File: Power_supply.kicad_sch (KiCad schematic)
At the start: 46 parts, among them U100 LM217MDT, U101 AMS1117-3.3, U102 AMS1117-3.3

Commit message: Sch update complete, ERC OK
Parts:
- removed Mod100: WB0524S-1W, Personal:WB___S-1W, symbol personal:WB____S-1W
- removed Mod101: WB0505S-1W, Personal:WB___S-1W, symbol personal:WB____S-1W
- added PS100: B0505S-2W, Personal:DCDC_converter_THT_BxxxxS-2W, symbol personal:B0505S-2W
- added PS101: B0524S-2W, Personal:DCDC_converter_THT_BxxxxS-2W, symbol personal:B0524S-2W
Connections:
- net GND: now also PS100.4 (-Vout)
- net SH0: now also PS100.2 (-Vin), PS101.2 (-Vin), PS101.4 (-Vout)
- net SH24: now also PS101.6 (+Vout)
- net SH5: now also PS100.1 (+Vin), PS101.1 (+Vin)
- net SL5: now also PS100.6 (+Vout)
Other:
- note removed: "Needs to be updated to 2W module"
- moved on the sheet: C100, C103, C105, C106, C108, R100, R101, U100, U102

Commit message: Placement 50%
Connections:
- no-connect marks 0 -> 2
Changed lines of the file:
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@@
 		(color 0 0 0 0)
 	)
+	(no_connect
+		(at 139.7 40.64)
+	)
+	(no_connect
+		(at 139.7 116.84)
+	)
+	(wire
+		(pts
+			(xy 138.43 40.64) (xy 139.7 40.64)
+		)
+		(stroke
+			(width 0)
+			(type default)
+		)
+	)
 	(wire
 		(pts
@@
 		(pts
 			(xy 101.6 74.93) (xy 101.6 76.2)
+		)
+		(stroke
+			(width 0)
+			(type default)
+		)
+	)
+	(wire
+		(pts
+			(xy 138.43 116.84) (xy 139.7 116.84)
 		)
 		(stroke
@@
 			(effects
 				(font
+					(size 1.27 1.27)
+					(italic yes)
+				)
+			)
+		)
+	)
+	(netclass_flag ""
+		(length 2.54)
+		(shape dot)
+		(at 139.7 116.84 270)
+		(effects
+			(font
+				(size 1.27 1.27)
+			)
+			(justify right bottom)
+		)
+		(property "Netclass" "LV"
+			(at 143.51 116.84 0)
+			(effects
+				(font
+					(size 1.27 1.27)
+				)
+				(justify left)
+			)
+		)
+		(property "Component Class" ""
+			(at -85.09 85.09 0)
+			(effects
+				(font

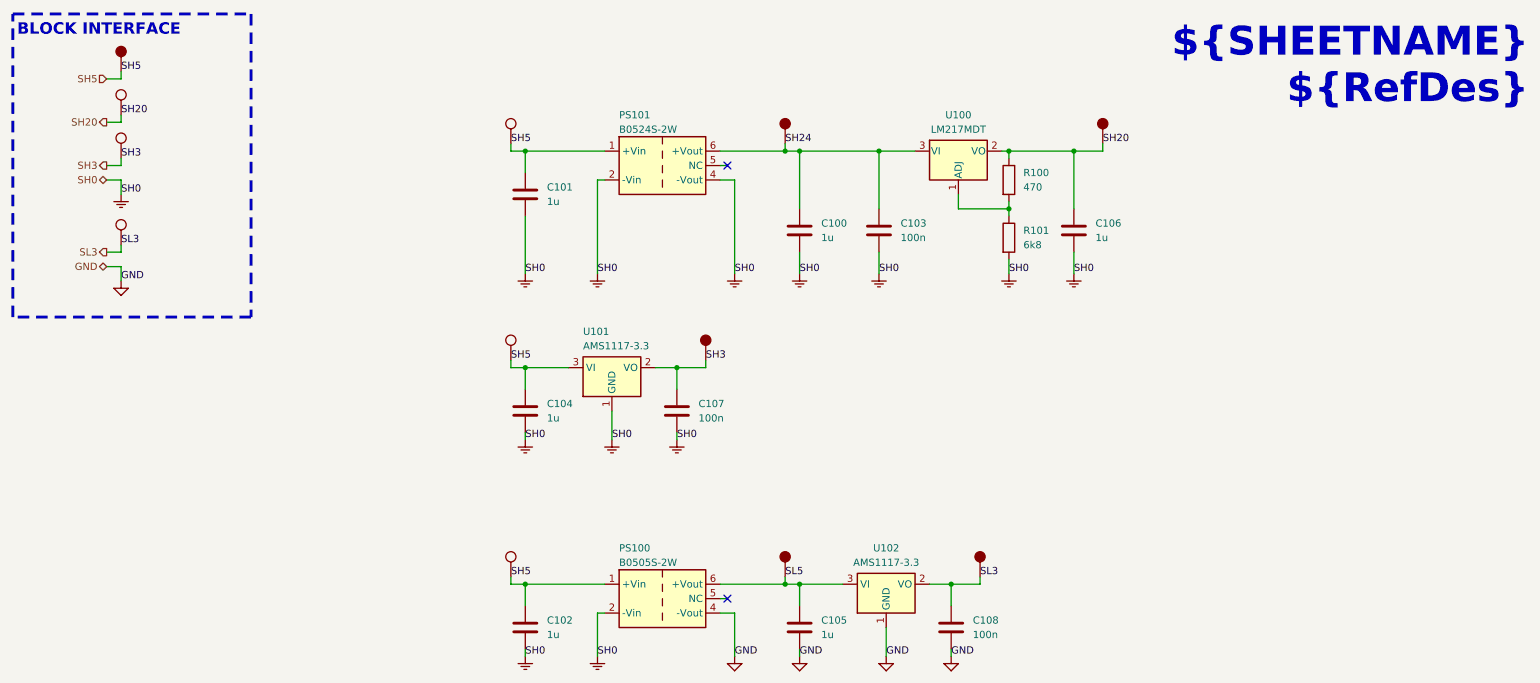
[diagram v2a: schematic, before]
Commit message: Reannotated, silk done, missing some 3D models
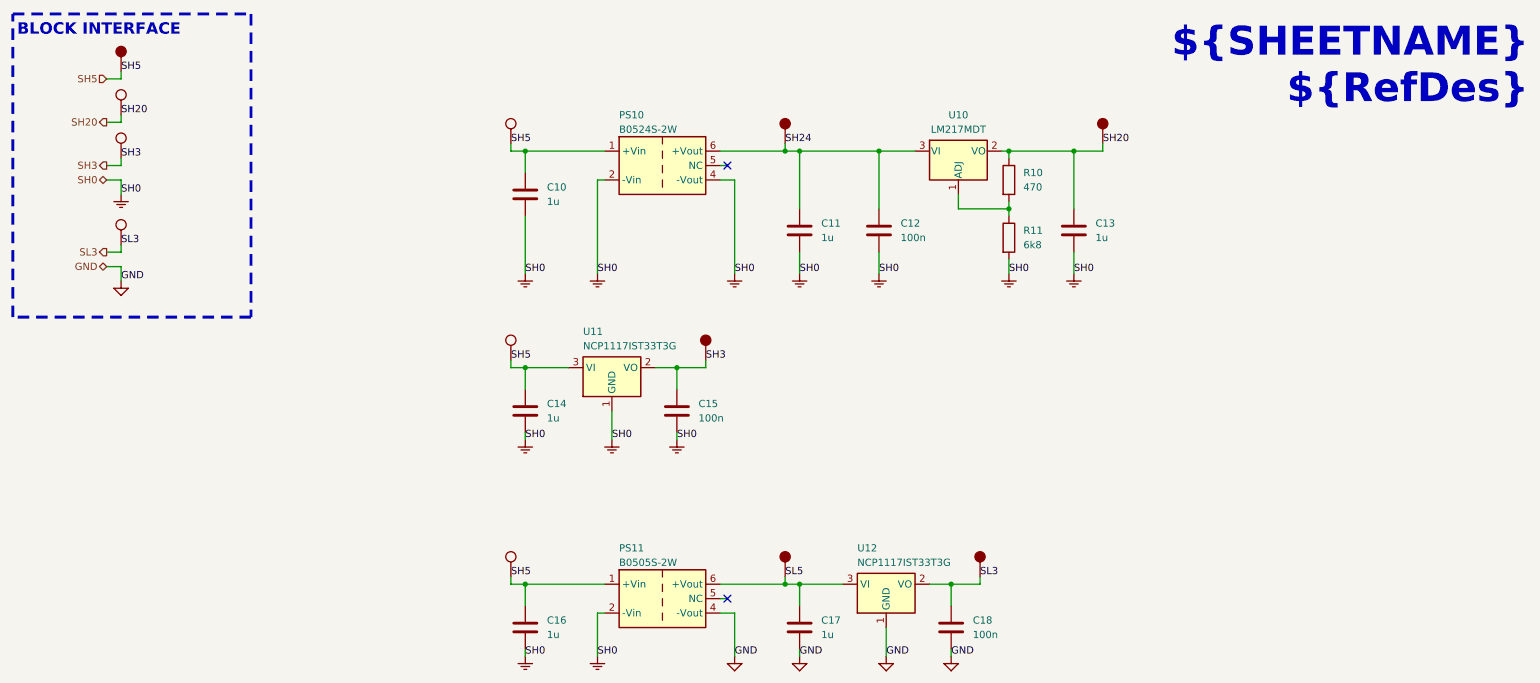
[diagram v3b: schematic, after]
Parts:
- removed U102: AMS1117-3.3, Package_TO_SOT_SMD:SOT-223-3_TabPin2, symbol Regulator_Linear:AMS1117-3.3
- added U12: NCP1117IST33T3G, Package_TO_SOT_SMD:SOT-223-3_TabPin2, symbol Regulator_Linear:AMS1117-3.3
- U11: renamed from U101; value AMS1117-3.3 -> NCP1117IST33T3G; Manufacturer UMW -> Onsemi; Manufacturer Part Number AMS1117-3.3 -> NCP1117IST33T3G
- renumbered C101 to C10, C100 to C11, C103 to C12, C106 to C13, C104 to C14, C107 to C15, C102 to C16, C105 to C17, C108 to C18, P100 to P32, P101 to P33, P107 to P34, P130 to P35, P123 to P36, P102 to P37, P103 to P38, P104 to P39, P110 to P40, P112 to P41, P115 to P42, P109 to P43, P114 to P44, P117 to P45, P122 to P46, P105 to P47, P118 to P48, P128 to P49, P120 to P50, P124 to P51, P126 to P52, P106 to P53, P119 to P54, P129 to P55, P111 to P56, P113 to P57, P116 to P58, P121 to P59, P125 to P60, P127 to P61, PS101 to PS10, PS100 to PS11, R100 to R10, R101 to R11, U100 to U10
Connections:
- net GND: now also U12.1 (GND)
- net SL3: now also U12.2 (VO)
- net SL5: now also U12.3 (VI)

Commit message: Changed to checked, updated fab pdf yaml
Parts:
- C10, C11, C13, C14, C16, C17, R10, R11: MAN (none) -> Generic
- C12, C15, C18: MAN (none) -> Generic; Manufacturer CCTC -> Generic; Manufacturer Part Number TCC0603X7R104K500CT -> (none)
- PS10: MAN (none) -> Evisun; MPN (none) -> B0524S-2W; Manufacturer (none) -> Evisun; Manufacturer Part Number (none) -> B0524S-2W
- PS11: MAN (none) -> Evisun; MPN (none) -> B0505S-2W; Manufacturer (none) -> Evisun; Manufacturer Part Number (none) -> B0505S-2W
- U10: MAN (none) -> ST; MPN (none) -> LM217MDT
- U11, U12: MAN (none) -> Onsemi; MPN (none) -> NCP1117IST33T3G
